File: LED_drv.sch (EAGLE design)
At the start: 17 parts, among them IC1 LM3409, T1 IRLR9343PBF

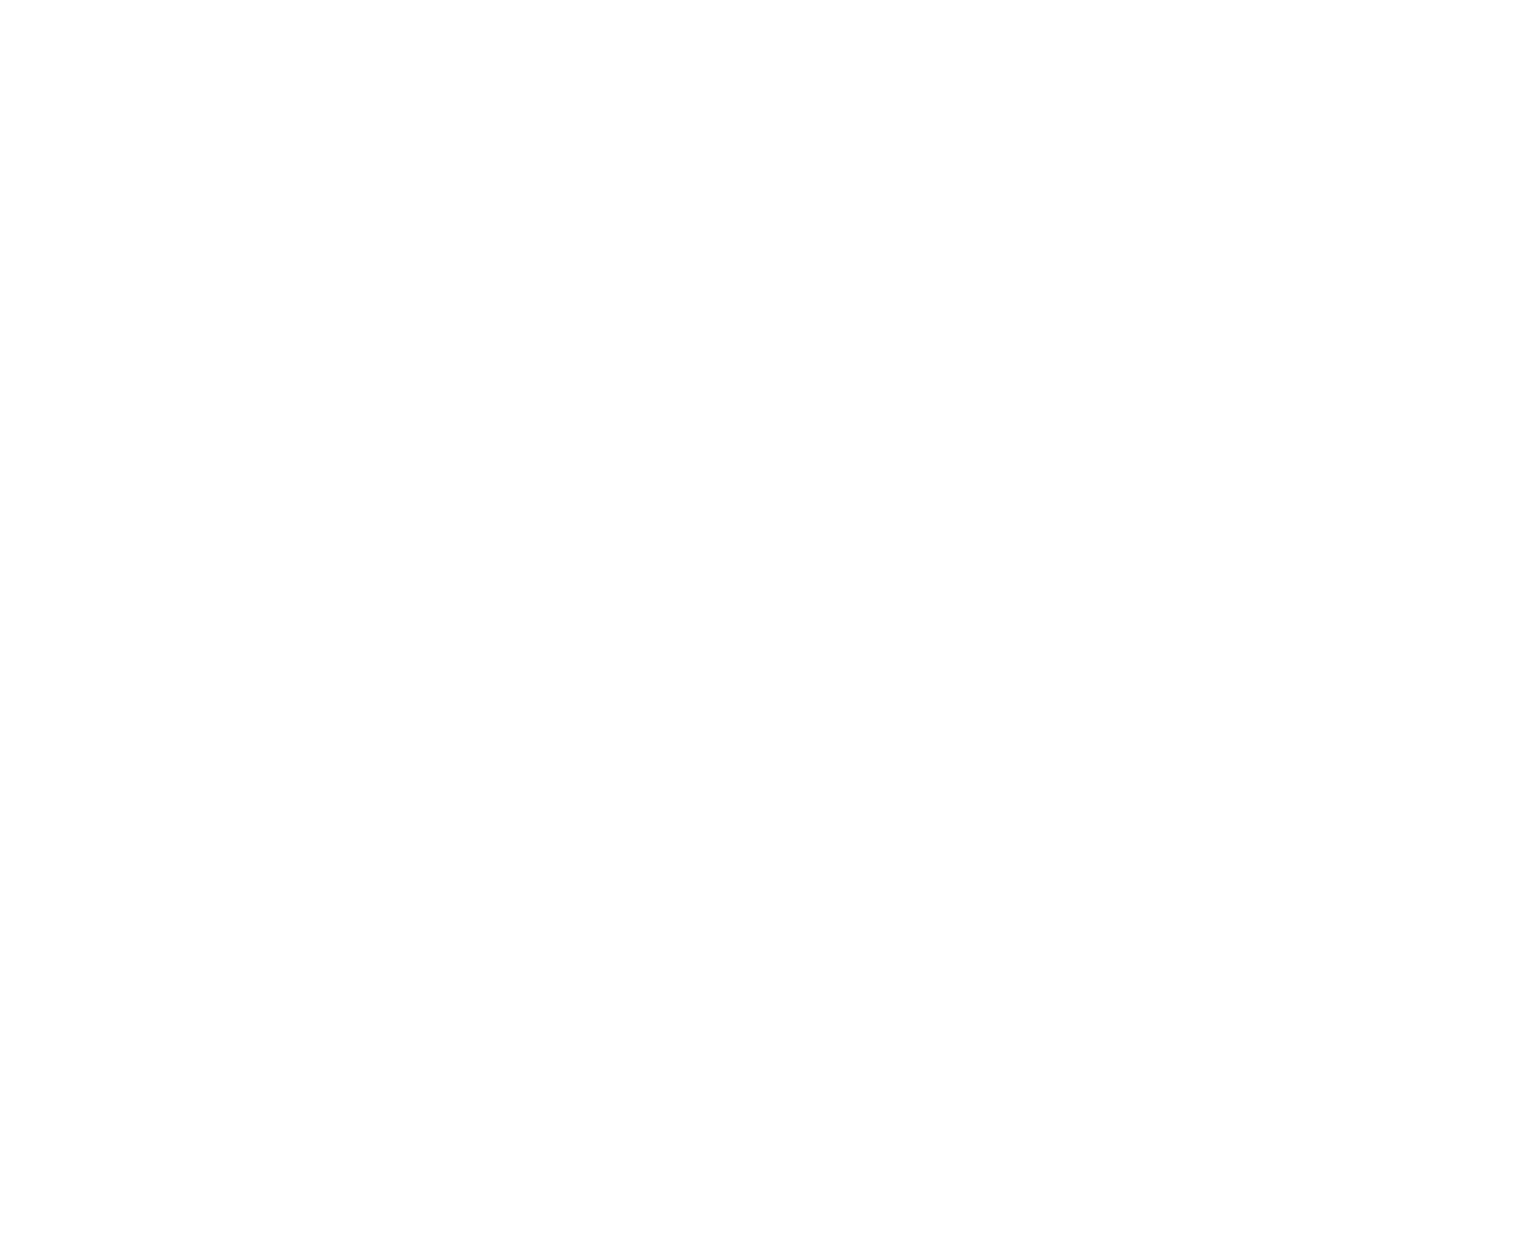
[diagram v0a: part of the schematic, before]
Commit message: Mains switch added
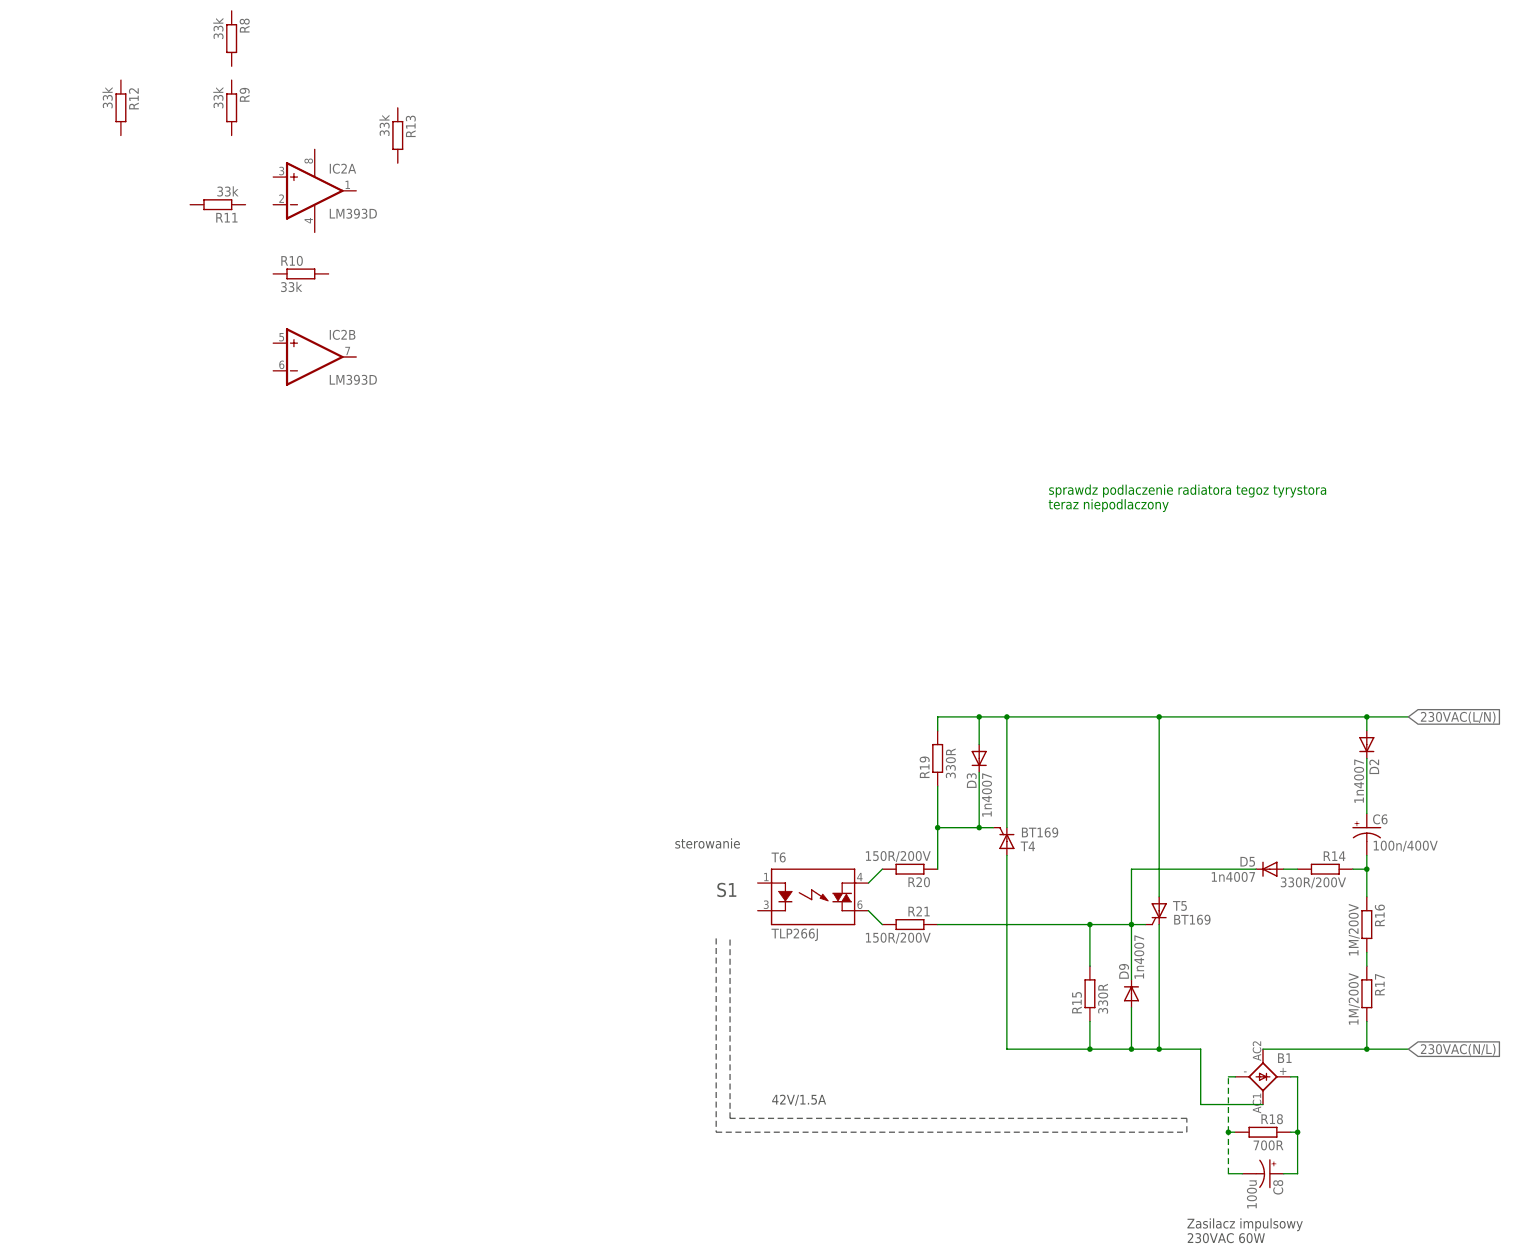
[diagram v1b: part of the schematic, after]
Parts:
- added B1: (no value), rectifier:FBP1,5
- added C6: 100n/400V, rcl:CPOL-USE3.5-8
- added C8: 100u, rcl:CPOL-USE3.5-8
- added D2, D3, D5, D9: 1n4007, diode:DIODE-DO-214AC
- added IC2: LM393D, linear:LM393D
- added R10, R11, R12, R13, R8, R9: 33k, resistor:R-EU_R0805
- added R14: 330R/200V, rcl:R-EU_R1206
- added R15, R19: 330R, rcl:R-EU_R1206
- added R16, R17: 1M/200V, rcl:R-EU_R1206
- added R18: 700R, rcl:R-EU_R1206
- added R20, R21: 150R/200V, rcl:R-EU_R1206
- added T4, T5: BT169, miscrel:BT169
- added T6: TLP266J, miscrel:TLP266J
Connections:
- new net 230VAC(L/N): D2.A, D3.A, R19.2, T4.C, T5.A
- new net 230VAC(N/L): B1.AC1, R17.2
- new net N$12: C6.-, R14.1, R16.1
- new net N$14: C6.+, D2.C
- new net N$15: D5.A, R14.2
- new net N$16: D5.C, D9.C, R15.2, R21.1, T5.G
- new net N$17: B1.+, C8.+, R18.1
- new net N$18: B1.-, C8.-, R18.2
- new net N$23: D3.C, R19.1, R20.1, T4.G
- new net N$24: B1.AC2, D9.A, R15.1, T4.A, T5.C
- new net N$25: R21.2, T6.DS2
- new net N$26: R20.2, T6.DS1
- new net N$7: R16.2, R17.1
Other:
- note added: "42V/1.5A"
- note added: "S1"
- note added: "Zasilacz impulsowy 230VAC 60W"
- note added: "sprawdz podlaczenie radiatora tegoz tyrystora teraz niepodlaczony"
- note added: "sterowanie"
